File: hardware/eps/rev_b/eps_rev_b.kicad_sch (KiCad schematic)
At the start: 0 parts

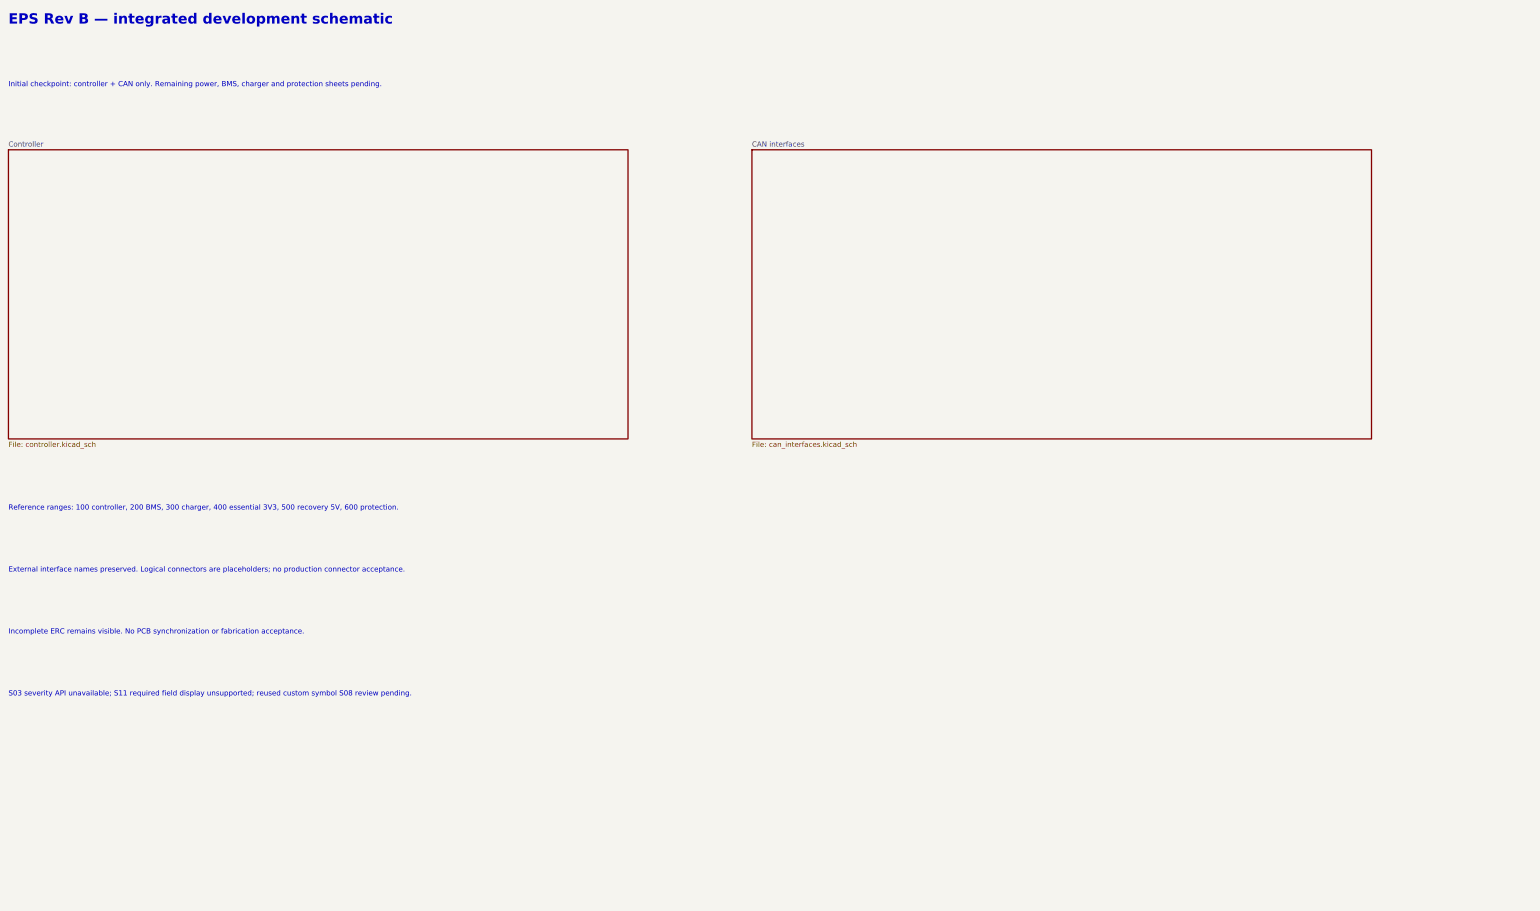
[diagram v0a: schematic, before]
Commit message: Integrate essential 3V3 buck into EPS Rev B
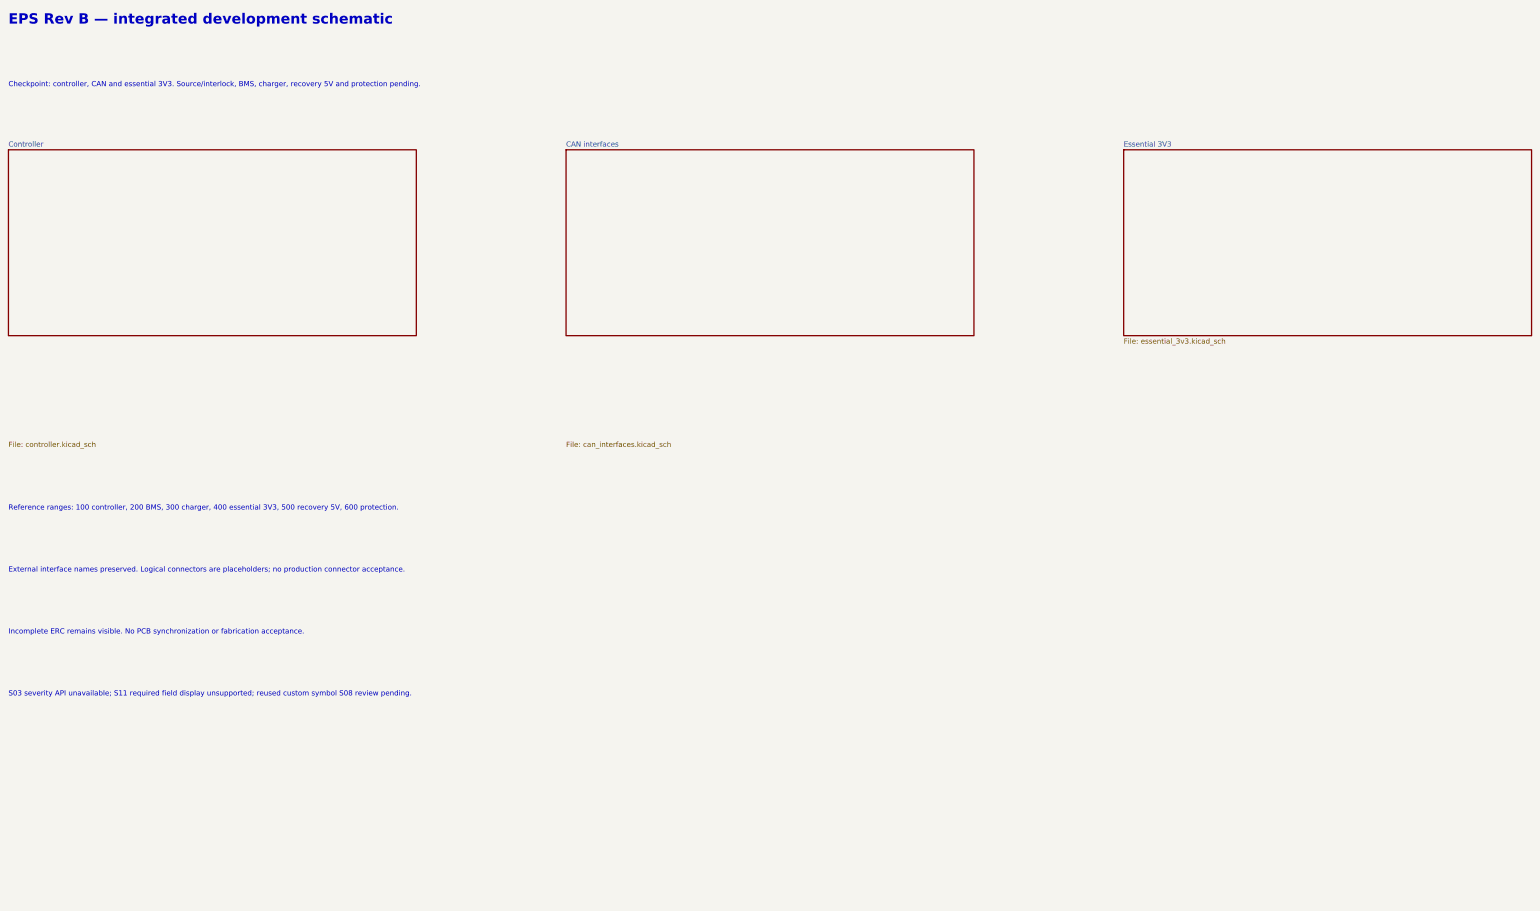
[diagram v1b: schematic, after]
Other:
- added sheet Essential 3V3 (essential_3v3.kicad_sch)
- note added: "Checkpoint: controller, CAN and essential 3V3. Source/interlock, BMS, charger, recovery 5V and protection pending."
- note removed: "Initial checkpoint: controller + CAN only. Remaining power, BMS, charger and protection sheets pending."
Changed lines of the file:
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@@
 	(paper "B")
 	(sheet
-    (at 30.48 60.96)
-    (size 152.4 71.12)
-    (fields_autoplaced yes)
-    (stroke (width 0.1524) (type solid))
-    (fill (color 0 0 0 0.0))
-    (property "Sheetname" "Controller"
-      (at 30.48 60.325 0)
-      (effects (font (size 1.27 1.27)) (justify left bottom))
-    )
-    (property "Sheetfile" "controller.kicad_sch"
-      (at 30.48 132.715 0)
-      (effects (font (size 1.27 1.27)) (justify left top))
-    )
-    (instances
-      (project "eps_rev_b"
-        (path "/8eba9f22-6f11-42d7-8e4a-b8de8905b113" (page "2"))
-      )
-    )
-  )
+		(at 30.48 60.96)
+		(size 100.33 45.72)
+		(fields_autoplaced)
+		(stroke
+			(width 0.1524)
+			(type solid)
+		)
+		(fill
+			(color 0 0 0 0.0)
+		)
+		(property "Sheetname" "Controller"
+			(at 30.48 60.325 0)
+			(effects
+				(font
+					(size 1.27 1.27)
+				)
+				(justify left bottom)
+			)
+		)
+		(property "Sheetfile" "controller.kicad_sch"
+			(at 30.48 132.715 0)
+			(effects
+				(font
+					(size 1.27 1.27)
+				)
+				(justify left top)
+			)
+		)
+		(instances
+			(project "eps_rev_b"
+				(path "/8eba9f22-6f11-42d7-8e4a-b8de8905b113"
+					(page "2")
+				)
+			)
+		)
+	)
 	(sheet
-    (at 213.36 60.96)
-    (size 152.4 71.12)
-    (fields_autoplaced yes)
-    (stroke (width 0.1524) (type solid))
-    (fill (color 0 0 0 0.0))
-    (property "Sheetname" "CAN interfaces"
-      (at 213.36 60.325 0)
-      (effects (font (size 1.27 1.27)) (justify left bottom))
-    )
-    (property "Sheetfile" "can_interfaces.kicad_sch"
-      (at 213.36 132.715 0)
-      (effects (font (size 1.27 1.27)) (justify left top))
-    )
-    (instances
-      (project "eps_rev_b"
-        (path "/8eba9f22-6f11-42d7-8e4a-b8de8905b113" (page "3"))
-      )
-    )
-  )
+		(at 167.64 60.96)
+		(size 100.33 45.72)
+		(fields_autoplaced)
+		(stroke
+			(width 0.1524)
+			(type solid)
+		)
+		(fill
+			(color 0 0 0 0.0)
+		)
+		(property "Sheetname" "CAN interfaces"
+			(at 167.64 60.325 0)
+			(effects
+				(font
+					(size 1.27 1.27)
+				)
+				(justify left bottom)
+			)
+		)
+		(property "Sheetfile" "can_interfaces.kicad_sch"
+			(at 167.64 132.715 0)
+			(effects
+				(font
+					(size 1.27 1.27)
+				)
+				(justify left top)
+			)
+		)
+		(instances
+			(project "eps_rev_b"
+				(path "/8eba9f22-6f11-42d7-8e4a-b8de8905b113"
+					(page "3")
+				)
+			)
+		)
+	)
   (text "EPS Rev B — integrated development schematic"
     (at 30.48 30.48 0)
     (effects (font (size 2.54 2.54) (bold yes)) (justify left bottom))
-  )
-  (text "Initial checkpoint: controller + CAN only. Remaining power, BMS, charger and protection sheets pending."
-    (at 30.48 45.72 0)
-    (effects (font (size 1.27 1.27)) (justify left bottom))
   )
   (text "Reference ranges: 100 controller, 200 BMS, 300 charger, 400 essential 3V3, 500 recovery 5V, 600 protection."
@@
     (effects (font (size 1.27 1.27)) (justify left bottom))
   )
+	(sheet
+    (at 304.8 60.96)
+    (size 100.33 45.72)
+    (fields_autoplaced yes)
+    (stroke (width 0.1524) (type solid))
+    (fill (color 0 0 0 0.0))
+    (property "Sheetname" "Essential 3V3"
+      (at 304.8 60.325 0)
+      (effects (font (size 1.27 1.27)) (justify left bottom))
+    )
+    (property "Sheetfile" "essential_3v3.kicad_sch"
+      (at 304.8 107.31500000000001 0)
+      (effects (font (size 1.27 1.27)) (justify left top))
+    )
+    (instances
+      (project "eps_rev_b"
+        (path "/8eba9f22-6f11-42d7-8e4a-b8de8905b113" (page "4"))
+      )
+    )
+  )
+  (text "Checkpoint: controller, CAN and essential 3V3. Source/interlock, BMS, charger, recovery 5V and protection pending."
+    (at 30.48 45.72 0)
+    (effects (font (size 1.27 1.27)) (justify left bottom))
+  )

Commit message: Integrate recovery converter with protected-rail boundary
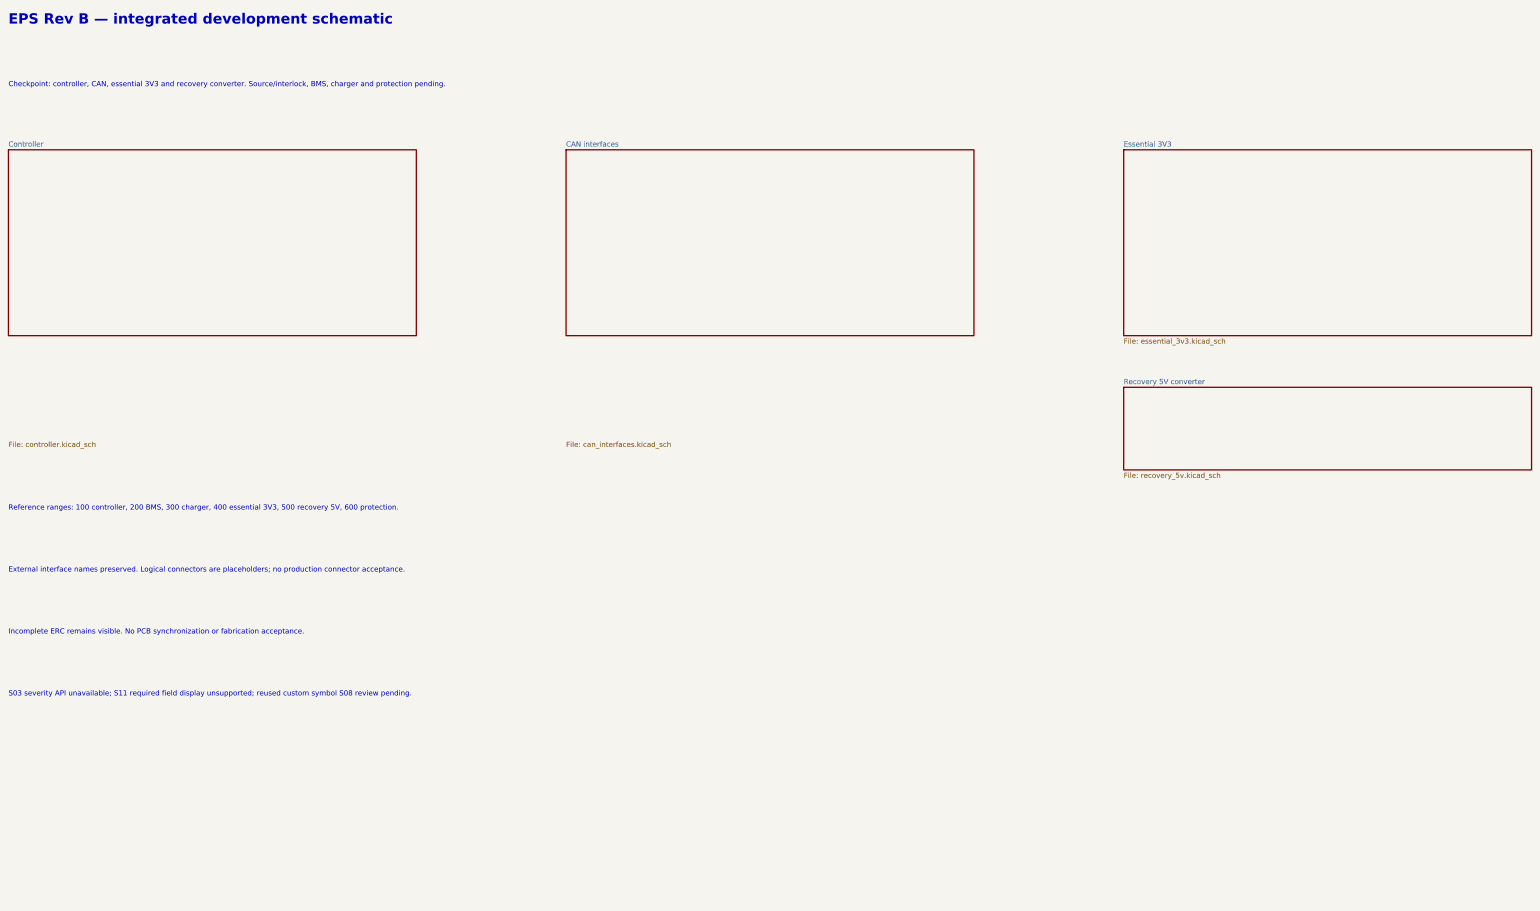
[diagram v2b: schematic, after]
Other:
- added sheet Recovery 5V converter (recovery_5v.kicad_sch)
- note added: "Checkpoint: controller, CAN, essential 3V3 and recovery converter. Source/interlock, BMS, charger and protection pending."
- note removed: "Checkpoint: controller, CAN and essential 3V3. Source/interlock, BMS, charger, recovery 5V and protection pending."
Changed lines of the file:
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@@
     )
   )
-  (text "Checkpoint: controller, CAN and essential 3V3. Source/interlock, BMS, charger, recovery 5V and protection pending."
+	(sheet
+    (at 304.8 119.38)
+    (size 100.33 20.32)
+    (fields_autoplaced yes)
+    (stroke (width 0.1524) (type solid))
+    (fill (color 0 0 0 0.0))
+    (property "Sheetname" "Recovery 5V converter"
+      (at 304.8 118.74499999999999 0)
+      (effects (font (size 1.27 1.27)) (justify left bottom))
+    )
+    (property "Sheetfile" "recovery_5v.kicad_sch"
+      (at 304.8 140.33499999999998 0)
+      (effects (font (size 1.27 1.27)) (justify left top))
+    )
+    (instances
+      (project "eps_rev_b"
+        (path "/8eba9f22-6f11-42d7-8e4a-b8de8905b113" (page "5"))
+      )
+    )
+  )
+  (text "Checkpoint: controller, CAN, essential 3V3 and recovery converter. Source/interlock, BMS, charger and protection pending."
     (at 30.48 45.72 0)
     (effects (font (size 1.27 1.27)) (justify left bottom))

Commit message: Integrate solar and recovery rail protection into EPS Rev B
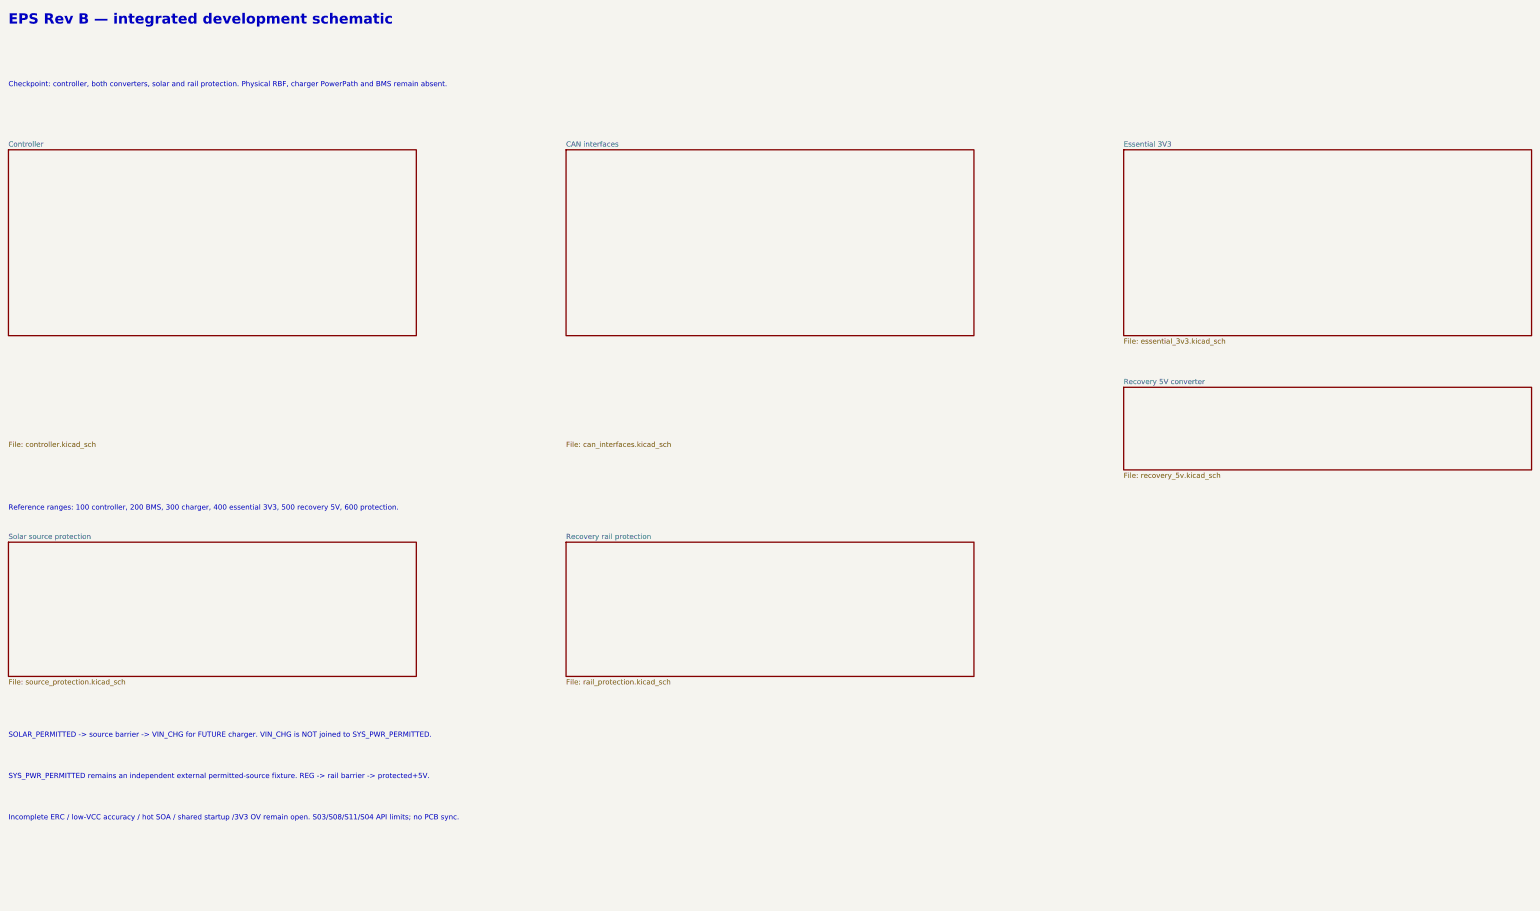
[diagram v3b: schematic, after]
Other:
- added sheet Recovery rail protection (rail_protection.kicad_sch)
- added sheet Solar source protection (source_protection.kicad_sch)
- note added: "Checkpoint: controller, both converters, solar and rail protection. Physical RBF, charger PowerPath and BMS remain absent."
- note added: "Incomplete ERC / low-VCC accuracy / hot SOA / shared startup /3V3 OV remain open. S03/S08/S11/S04 API limits; no PCB sync."
- note added: "SOLAR_PERMITTED -> source barrier -> VIN_CHG for FUTURE charger. VIN_CHG is NOT joined to SYS_PWR_PERMITTED."
- note added: "SYS_PWR_PERMITTED remains an independent external permitted-source fixture. REG -> rail barrier -> protected+5V."
- note removed: "Checkpoint: controller, CAN, essential 3V3 and recovery converter. Source/interlock, BMS, charger and protection pending."
- note removed: "External interface names preserved. Logical connectors are placeholders; no production connector acceptance."
- note removed: "Incomplete ERC remains visible. No PCB synchronization or fabrication acceptance."
- note removed: "S03 severity API unavailable; S11 required field display unsupported; reused custom symbol S08 review pending."
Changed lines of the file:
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@@
-    (effects (font (size 1.27 1.27)) (justify left bottom))
-  )
-  (text "External interface names preserved. Logical connectors are placeholders; no production connector acceptance."
-    (at 30.48 165.1 0)
-    (effects (font (size 1.27 1.27)) (justify left bottom))
-  )
-  (text "Incomplete ERC remains visible. No PCB synchronization or fabrication acceptance."
-    (at 30.48 180.34 0)
-    (effects (font (size 1.27 1.27)) (justify left bottom))
-  )
-  (text "S03 severity API unavailable; S11 required field display unsupported; reused custom symbol S08 review pending."
-    (at 30.48 195.58 0)
     (effects (font (size 1.27 1.27)) (justify left bottom))
   )
@@
     )
   )
-  (text "Checkpoint: controller, CAN, essential 3V3 and recovery converter. Source/interlock, BMS, charger and protection pending."
+	(sheet
+    (at 30.48 157.48)
+    (size 100.33 33.02)
+    (fields_autoplaced yes)
+    (stroke (width 0.1524) (type solid))
+    (fill (color 0 0 0 0.0))
+    (property "Sheetname" "Solar source protection"
+      (at 30.48 156.845 0)
+      (effects (font (size 1.27 1.27)) (justify left bottom))
+    )
+    (property "Sheetfile" "source_protection.kicad_sch"
+      (at 30.48 191.135 0)
+      (effects (font (size 1.27 1.27)) (justify left top))
+    )
+    (instances
+      (project "eps_rev_b"
+        (path "/8eba9f22-6f11-42d7-8e4a-b8de8905b113" (page "6"))
+      )
+    )
+  )
+	(sheet
+    (at 167.64 157.48)
+    (size 100.33 33.02)
+    (fields_autoplaced yes)
+    (stroke (width 0.1524) (type solid))
+    (fill (color 0 0 0 0.0))
+    (property "Sheetname" "Recovery rail protection"
+      (at 167.64 156.845 0)
+      (effects (font (size 1.27 1.27)) (justify left bottom))
+    )
+    (property "Sheetfile" "rail_protection.kicad_sch"
+      (at 167.64 191.135 0)
+      (effects (font (size 1.27 1.27)) (justify left top))
+    )
+    (instances
+      (project "eps_rev_b"
+        (path "/8eba9f22-6f11-42d7-8e4a-b8de8905b113" (page "7"))
+      )
+    )
+  )
+  (text "Checkpoint: controller, both converters, solar and rail protection. Physical RBF, charger PowerPath and BMS remain absent."
     (at 30.48 45.72 0)
     (effects (font (size 1.27 1.27)) (justify left bottom))
   )
+  (text "SOLAR_PERMITTED -> source barrier -> VIN_CHG for FUTURE charger. VIN_CHG is NOT joined to SYS_PWR_PERMITTED."
+    (at 30.48 205.74 0)
+    (effects (font (size 1.27 1.27)) (justify left bottom))
+  )
+  (text "SYS_PWR_PERMITTED remains an independent external permitted-source fixture. REG -> rail barrier -> protected+5V."
+    (at 30.48 215.9 0)
+    (effects (font (size 1.27 1.27)) (justify left bottom))
+  )
+  (text "Incomplete ERC / low-VCC accuracy / hot SOA / shared startup /3V3 OV remain open. S03/S08/S11/S04 API limits; no PCB sync."
+    (at 30.48 226.06 0)
+    (effects (font (size 1.27 1.27)) (justify left bottom))
+  )
